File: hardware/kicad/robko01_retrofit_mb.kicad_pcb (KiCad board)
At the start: 2 copper layers, 178.8 x 143.8 mm, 80 parts, among them J1 Conn_01x04_Pin, J10 Motors, J11 Motors, J12 Conn_01x04_Pin, J13 Conn_01x02_Pin, J14 Conn_01x04_Pin, J15 Conn_01x02_Pin, J16 Conn_01x04_Pin, J17 Conn_01x02_Male, J18 Conn_01x06_Pin, J19 TP-GND, J2 Conn_01x02_Pin, J21 Conn_01x19_Pin, J22 Conn_01x19_Pin, J23 Conn_02x05_Odd_Even, J24 USB_A, J25 USB_B, J28 Conn_01x02_Male, J3 Conn_01x02_Pin, J31 Conn_02x05_Odd_Even, J4 Conn_01x04_Pin, J5 Conn_01x02_Pin, J6 Conn_01x04_Pin, J7 Conn_01x02_Male, J8 Conn_01x02_Pin, J9 Motors, K2 G5V-2, SW1 SW_DIP_x04, SW2 SW_DIP_x04, SW3 SW_DIP_x04, SW4 SW_DIP_x04, SW5 SW_DIP_x04, SW6 RESET, SW7 SW_DIP_x04, U1 LM7805_TO220, U2 PC817

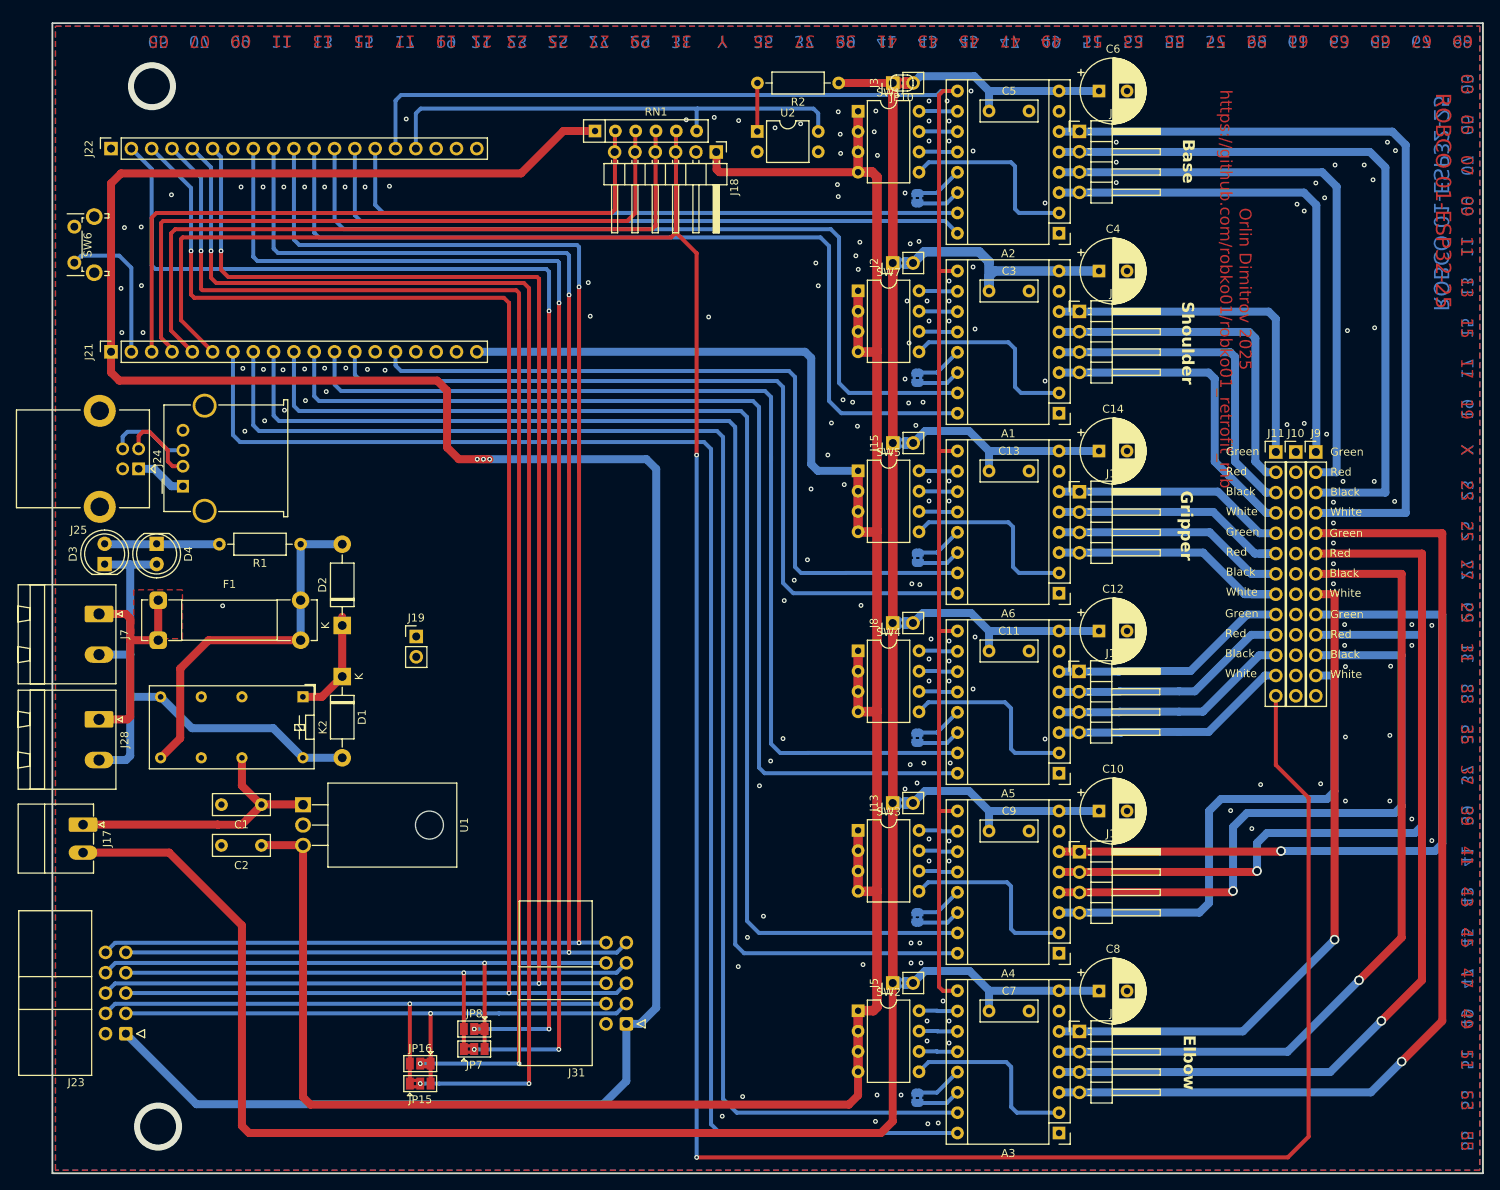
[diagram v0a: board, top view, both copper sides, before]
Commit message: Convert ceramic capacitors to 0805 footprints
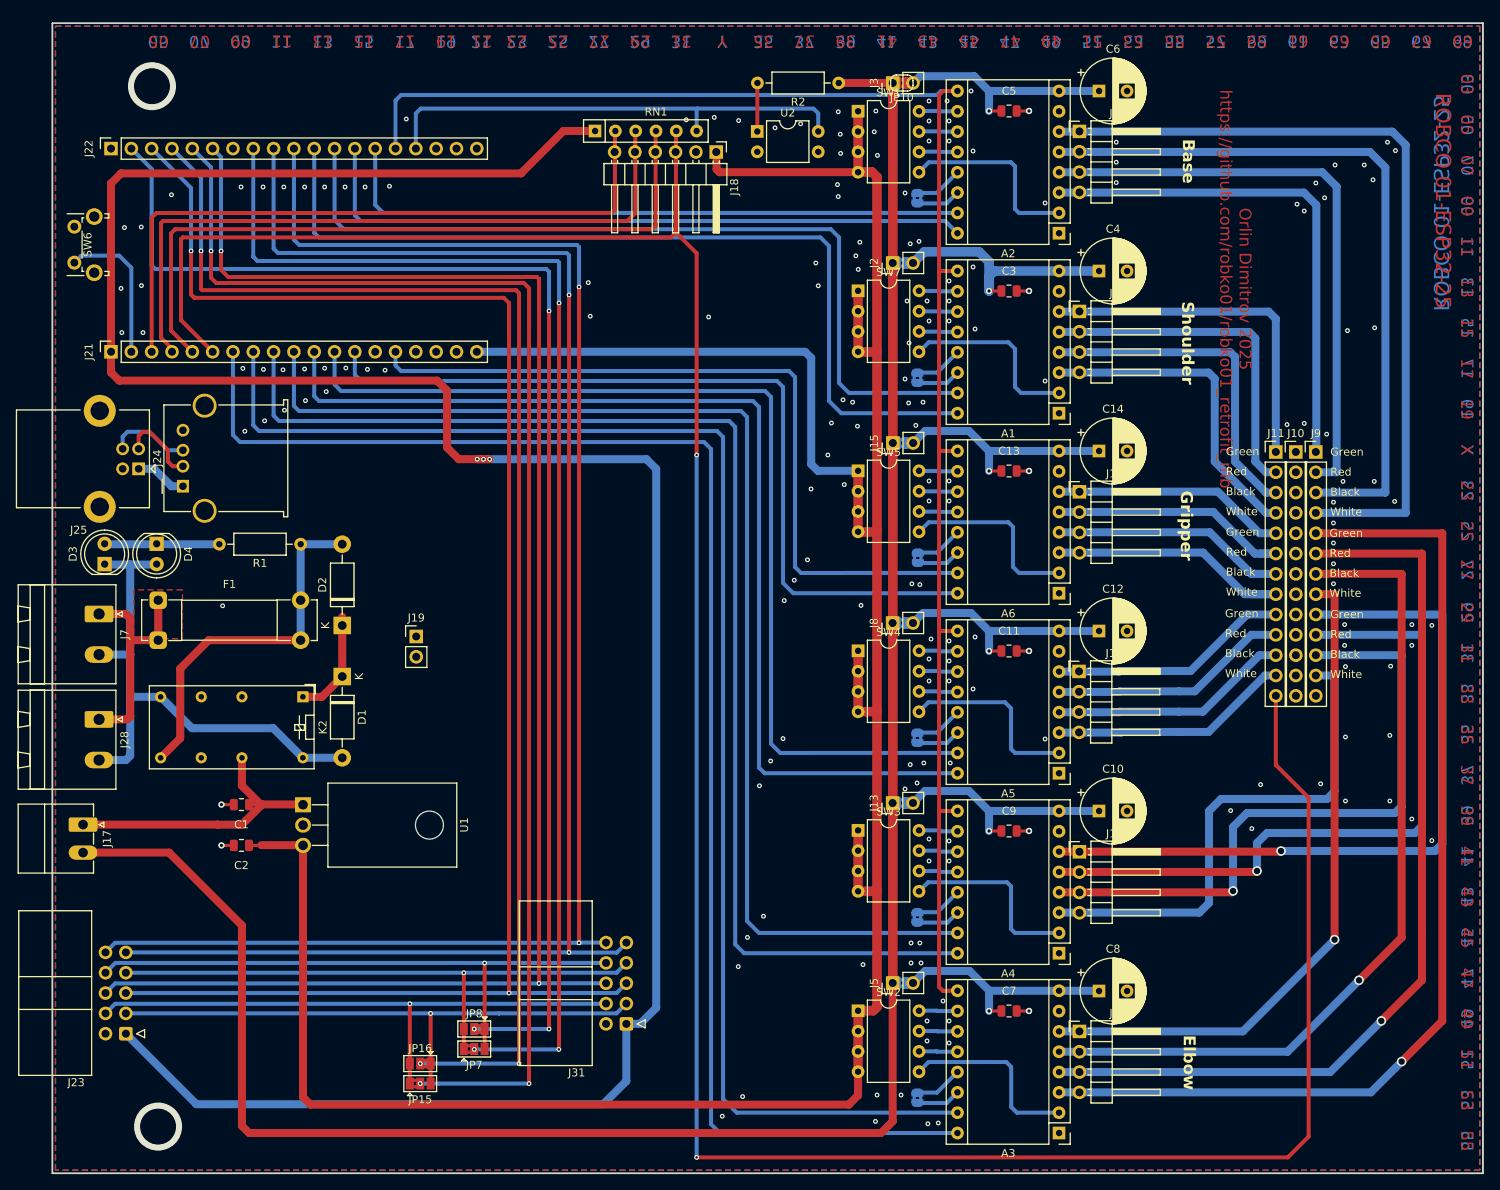
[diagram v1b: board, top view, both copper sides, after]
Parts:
- C1, C11, C13, C2, C3, C5, C7, C9: footprint Capacitor_THT:C_Disc_D7.0mm_W2.5mm_P5.00mm -> Capacitor_SMD:C_0805_2012Metric
- moved C1 2.50 mm to (62.8, 114.2)
- moved C11 2.50 mm to (158.8, 95.0)
- moved C13 2.50 mm to (158.8, 72.5)
- moved C2 2.50 mm to (62.8, 119.3)
- moved C3 2.50 mm to (158.8, 50.0)
- moved C5 2.50 mm to (158.8, 27.5)
- moved C7 2.50 mm to (158.8, 140.0)
- moved C9 2.50 mm to (158.8, 117.5)
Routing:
- net GND: track 0.00 -> 12.4 mm, vias 177 -> 185
- net Net-(A6-VMOT): track 27.4 -> 28.9 mm, vias 0 -> 1
- net Net-(A5-VMOT): track 27.2 -> 28.7 mm, vias 0 -> 1
- net Net-(A4-VMOT): track 27.4 -> 29.0 mm, vias 0 -> 1
- net Net-(A3-VMOT): track 27.4 -> 29.0 mm, vias 0 -> 1
- net Net-(A2-VMOT): track 26.9 -> 28.4 mm, vias 0 -> 1
- net Net-(A1-VMOT): track 30.1 -> 31.7 mm, vias 0 -> 1
- net +5V: track 355.9 -> 357.4 mm
- net VCC: track 35.5 -> 37.0 mm

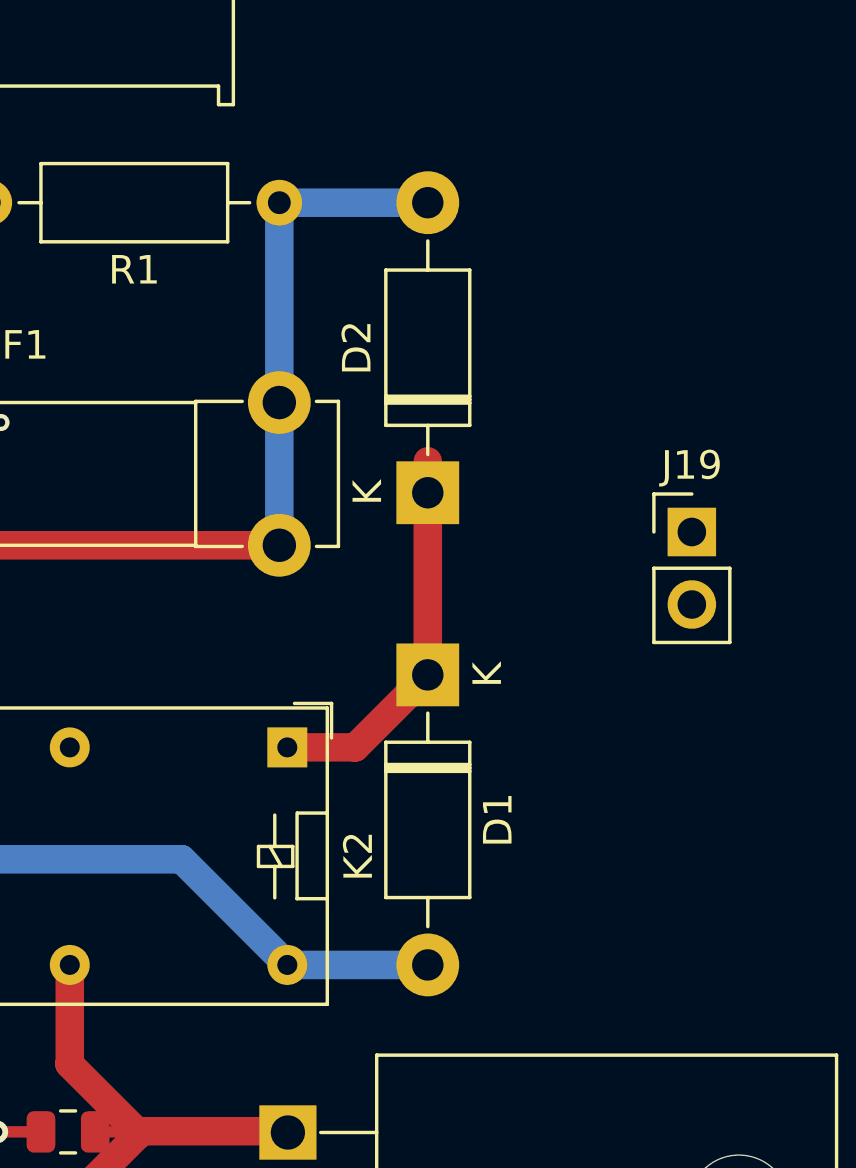
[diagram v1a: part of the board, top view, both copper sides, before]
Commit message: Convert D1 and D2 to SMD and remove obsolete BOM snapshots
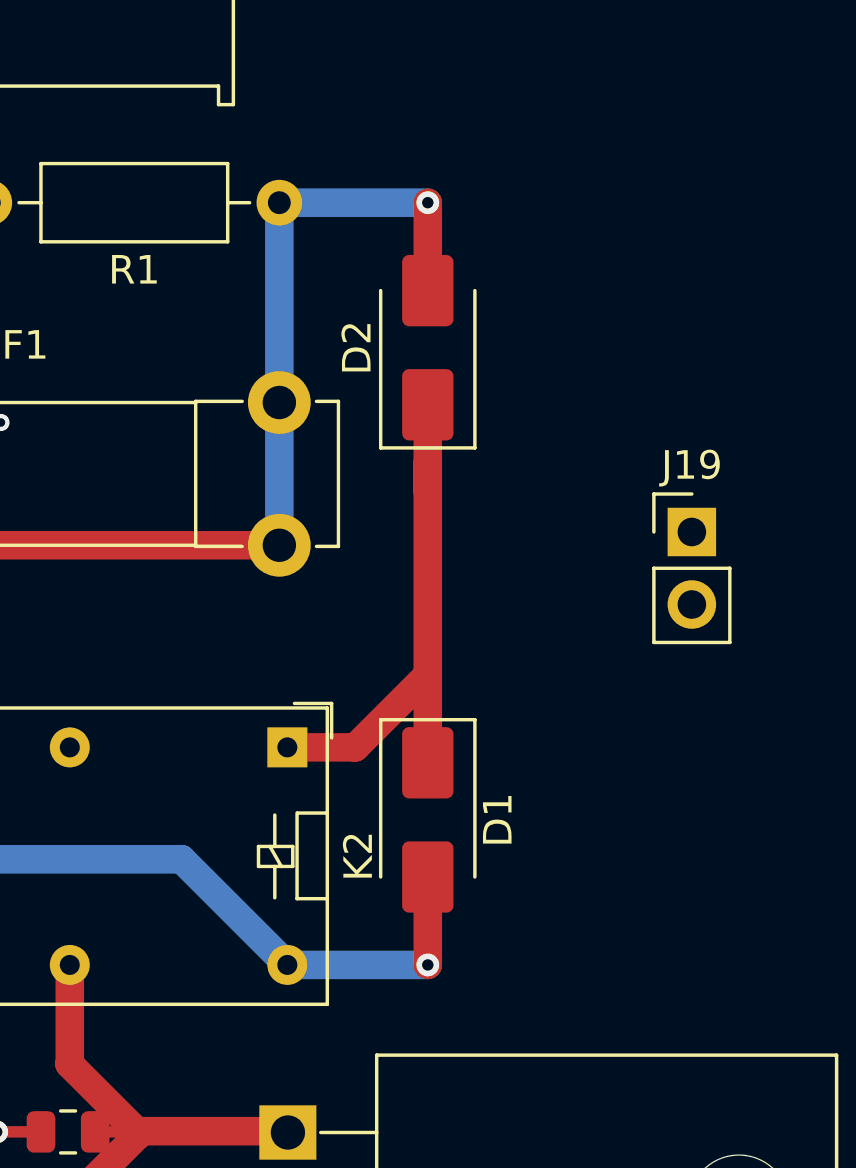
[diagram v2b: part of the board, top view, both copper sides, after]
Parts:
- D1, D2: value 1N4007 -> S1M; footprint Diode_THT:D_DO-41_SOD81_P10.16mm_Horizontal -> Diode_SMD:D_SMA
- moved D1 5.08 mm to (75.4, 103.3)
- moved D2 5.08 mm to (75.4, 86.7)
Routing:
- net Net-(D1-K): track 13.5 -> 19.6 mm
- net Net-(D2-A): track 45.9 -> 49.0 mm, vias 0 -> 1
- net Net-(D1-A): track 68.1 -> 71.2 mm, vias 0 -> 1

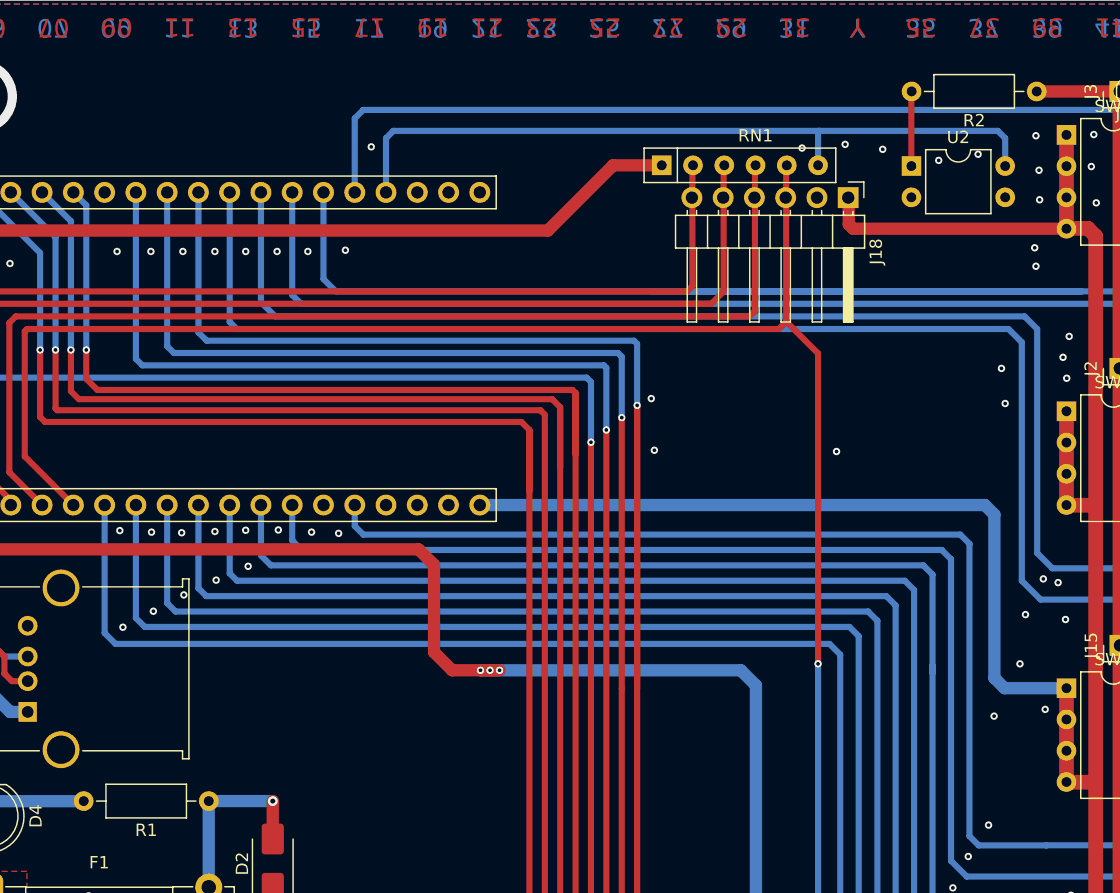
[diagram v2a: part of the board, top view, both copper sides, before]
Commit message: Convert resistors to 0805 and split RN1 into five 10k resistors
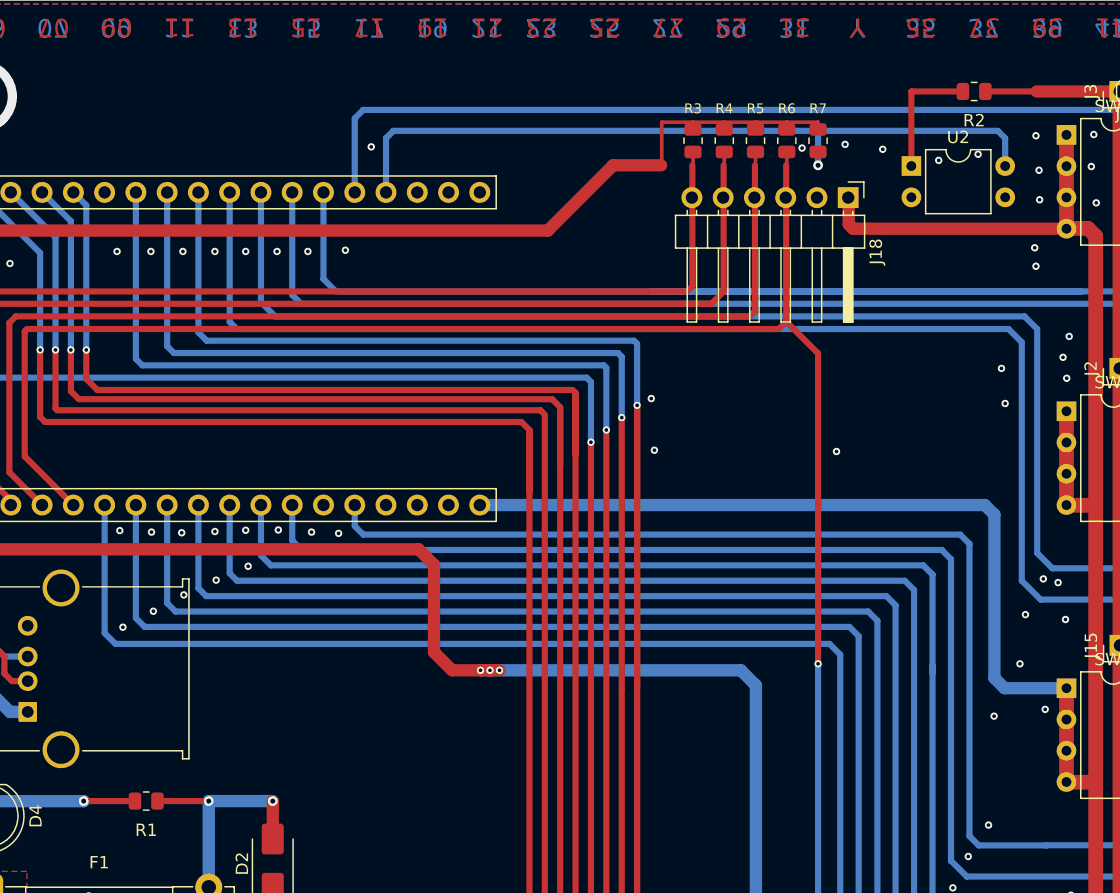
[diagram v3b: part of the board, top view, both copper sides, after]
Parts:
- removed RN1: R_Network05, Resistor_THT:R_Array_SIP6
- added R3: 10k, Resistor_SMD:R_0805_2012Metric, F.Cu at (109.5, 28.0)
- added R4: 10k, Resistor_SMD:R_0805_2012Metric, F.Cu at (112.1, 28.0)
- added R5: 10k, Resistor_SMD:R_0805_2012Metric, F.Cu at (114.6, 28.0)
- added R6: 10k, Resistor_SMD:R_0805_2012Metric, F.Cu at (117.2, 28.0)
- added R7: 10k, Resistor_SMD:R_0805_2012Metric, F.Cu at (119.7, 28.0)
- R1, R2: footprint Resistor_THT:R_Axial_DIN0207_L6.3mm_D2.5mm_P10.16mm_Horizontal -> Resistor_SMD:R_0805_2012Metric
- moved R2 5.08 mm to (132.4, 24.0)
- moved R1 5.08 mm to (65.1, 81.7)
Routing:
- net +3.3V: track 312.1 -> 331.3 mm
- net MC_POWER: track 267.6 -> 271.7 mm
- net Net-(D2-A): track 49.0 -> 53.1 mm, vias 1 -> 2
- net Net-(R2-Pad2): track 6.07 -> 10.2 mm
- net Net-(D3-A): track 14.3 -> 18.5 mm, vias 0 -> 1
- net M6-Limit: track 342.1 -> 343.2 mm
- net M3-Limit: track 84.9 -> 86.0 mm
- net M2-Limit: track 86.7 -> 87.8 mm
- net E-STOP: track 60.3 -> 61.4 mm, vias 0 -> 1
- net M1-Limit: track 88.7 -> 89.8 mm

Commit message: Convert D3 and D4 to 0805 LED footprints
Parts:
- D3: value LED 3mm Green -> LED 0805 Green; footprint LED_THT:LED_D5.0mm -> LED_SMD:LED_0805_2012Metric
- D4: value LED 3mm Red -> LED 0805 Red; footprint LED_THT:LED_D5.0mm -> LED_SMD:LED_0805_2012Metric
- moved D4 1.27 mm to (52.2, 82.9)
- moved D3 1.27 mm to (45.7, 82.9)
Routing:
- net Net-(D3-A): track 18.5 -> 19.2 mm, vias 1 -> 3
- net Net-(D1-A): track 71.2 -> 71.8 mm, vias 1 -> 3
